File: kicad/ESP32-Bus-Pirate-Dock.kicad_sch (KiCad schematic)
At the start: 11 parts, among them J1 Conn_01x10, J4 Conn_01x22_MountingPin, J5 Conn_01x22_MountingPin, SW1 SW_BOOT, SW2 SW_RST, U1 ESP32-S3-DEVKITC-1-N8R2, U2 AMS1117-1.8

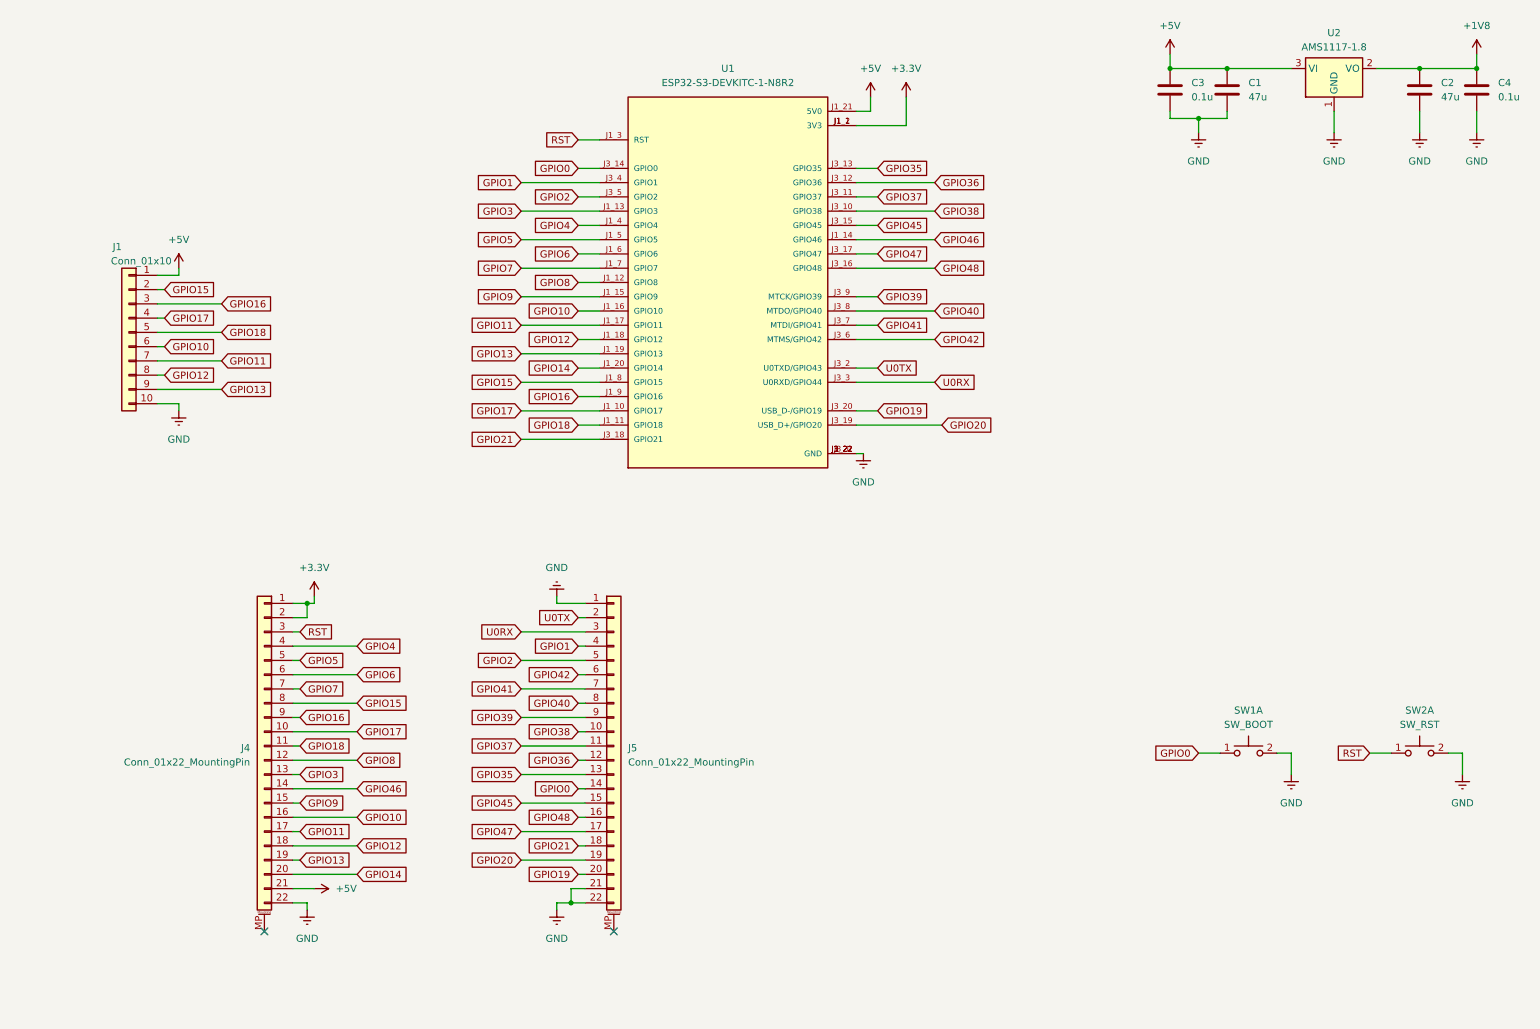
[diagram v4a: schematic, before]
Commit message: Added logic level shifting
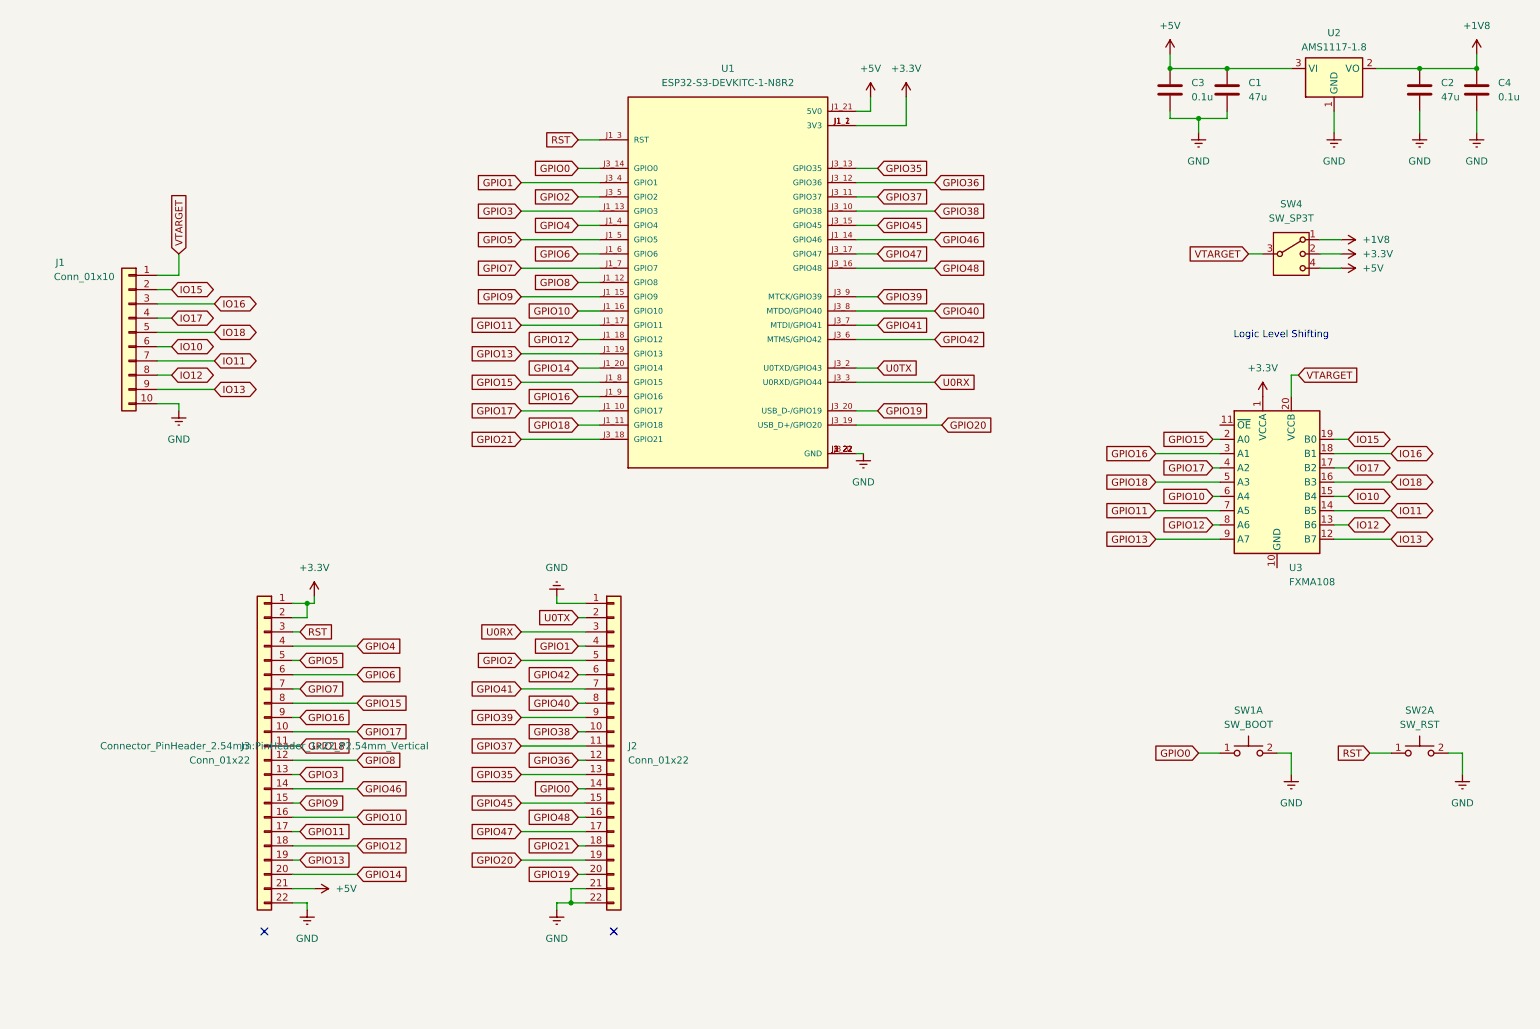
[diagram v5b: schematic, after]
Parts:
- removed J4, J5: Conn_01x22_MountingPin, Connector_PinHeader_2.54mm:PinHeader_1x22_P2.54mm_Vertical, symbol Connector_Generic_MountingPin:Conn_01x22_MountingPin
- added J2, J3: Conn_01x22, Connector_PinHeader_2.54mm:PinHeader_1x22_P2.54mm_Vertical, symbol Connector_Generic:Conn_01x22
- added SW4: SW_SP3T, Button_Switch_SMD:SW_SP3T_PCM13, symbol Switch:SW_SP3T
- added U3: FXMA108, Package_DFN_QFN:WQFN-20-1EP_2.5x4.5mm_P0.5mm_EP1x2.9mm, symbol Logic_LevelTranslator:FXMA108
- J1: footprint Connector_PinSocket_2.54mm:PinSocket_1x10_P2.54mm_Horizontal -> Connector_PinSocket_2.54mm:PinSocket_1x10_P2.54mm_Vertical
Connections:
- net +1V8: now also SW4.1
- net +3.3V: now also J3.1 (Pin_1), J3.2 (Pin_2), SW4.2, U3.1 (VCCA)
- net +5V: now also J3.21 (Pin_21), SW4.4; no longer J1.1 (Pin_1)
- net GND: now also J2.1 (Pin_1), J2.21 (Pin_21), J2.22 (Pin_22), J3.22 (Pin_22)
- net GPIO0: now also J2.14 (Pin_14)
- net GPIO1: now also J2.4 (Pin_4)
- net GPIO10: now also J3.16 (Pin_16), U3.6 (A4); no longer J1.6 (Pin_6)
- net GPIO11: now also J3.17 (Pin_17), U3.7 (A5); no longer J1.7 (Pin_7)
- net GPIO12: now also J3.18 (Pin_18), U3.8 (A6); no longer J1.8 (Pin_8)
- net GPIO13: now also J3.19 (Pin_19), U3.9 (A7); no longer J1.9 (Pin_9)
- net GPIO14: now also J3.20 (Pin_20)
- net GPIO15: now also J3.8 (Pin_8), U3.2 (A0); no longer J1.2 (Pin_2)
- net GPIO16: now also J3.9 (Pin_9), U3.3 (A1); no longer J1.3 (Pin_3)
- net GPIO17: now also J3.10 (Pin_10), U3.4 (A2); no longer J1.4 (Pin_4)
- net GPIO18: now also J3.11 (Pin_11), U3.5 (A3); no longer J1.5 (Pin_5)
- net GPIO19: now also J2.20 (Pin_20)
- net GPIO2: now also J2.5 (Pin_5)
- net GPIO20: now also J2.19 (Pin_19)
- net GPIO21: now also J2.18 (Pin_18)
- net GPIO3: now also J3.13 (Pin_13)
- net GPIO35: now also J2.13 (Pin_13)
- net GPIO36: now also J2.12 (Pin_12)
- net GPIO37: now also J2.11 (Pin_11)
- net GPIO38: now also J2.10 (Pin_10)
- net GPIO39: now also J2.9 (Pin_9)
- net GPIO4: now also J3.4 (Pin_4)
- net GPIO40: now also J2.8 (Pin_8)
- net GPIO41: now also J2.7 (Pin_7)
- net GPIO42: now also J2.6 (Pin_6)
- net GPIO45: now also J2.15 (Pin_15)
- net GPIO46: now also J3.14 (Pin_14)
- net GPIO47: now also J2.17 (Pin_17)
- net GPIO48: now also J2.16 (Pin_16)
- net GPIO5: now also J3.5 (Pin_5)
- net GPIO6: now also J3.6 (Pin_6)
- net GPIO7: now also J3.7 (Pin_7)
- net GPIO8: now also J3.12 (Pin_12)
- net GPIO9: now also J3.15 (Pin_15)
- net RST: now also J3.3 (Pin_3)
- net U0RX: now also J2.3 (Pin_3)
- net U0TX: now also J2.2 (Pin_2)
- new net IO10: J1.6 (Pin_6), U3.15 (B4)
- new net IO11: J1.7 (Pin_7), U3.14 (B5)
- new net IO12: J1.8 (Pin_8), U3.13 (B6)
- new net IO13: J1.9 (Pin_9), U3.12 (B7)
- new net IO15: J1.2 (Pin_2), U3.19 (B0)
- new net IO16: J1.3 (Pin_3), U3.18 (B1)
- new net IO17: J1.4 (Pin_4), U3.17 (B2)
- new net IO18: J1.5 (Pin_5), U3.16 (B3)
- new net VTARGET: J1.1 (Pin_1), SW4.3, U3.20 (VCCB)
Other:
- note added: "Logic Level Shifting"

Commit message: PCB modifications
- removed RESET switch
- re-arranged FXMA108 pins
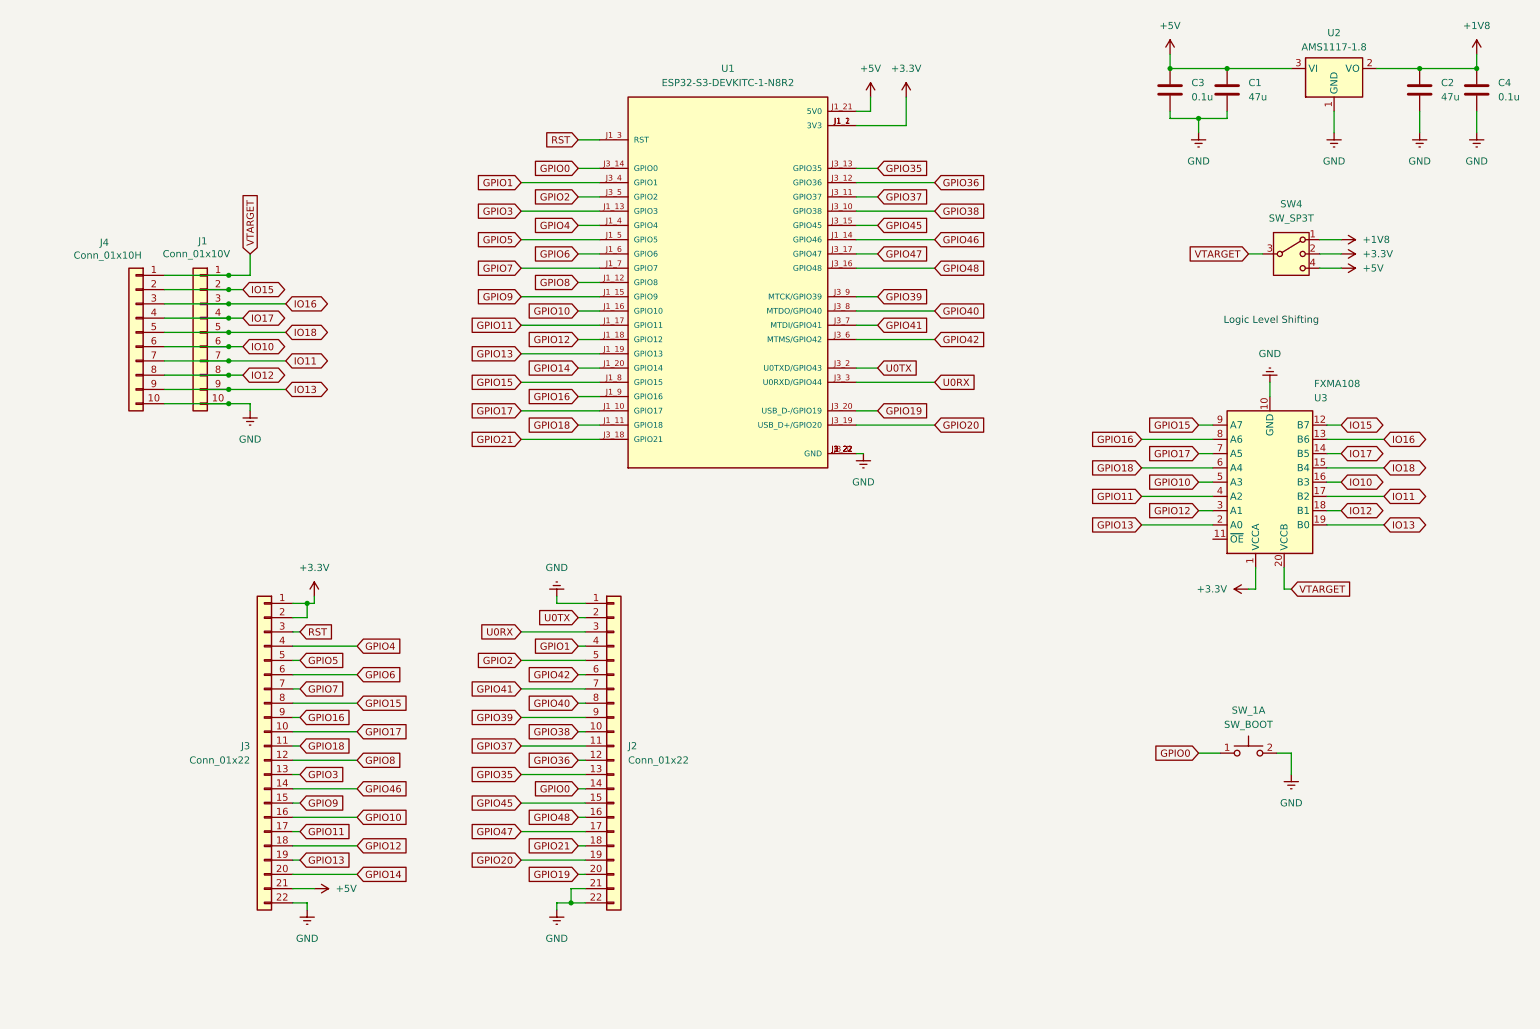
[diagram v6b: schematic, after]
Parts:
- removed SW2: SW_RST, symbol Switch:SW_Push_Dual_x2
- added J4: Conn_01x10H, Connector_PinSocket_2.54mm:PinSocket_1x10_P2.54mm_Horizontal, symbol Connector_Generic:Conn_01x10
- J1: value Conn_01x10 -> Conn_01x10V
- SW_1: renamed from SW1; footprint (none) -> Button_Switch_SMD:SW_SPST_PTS647_Sx50
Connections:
- net GND: now also U3.10 (GND), J4.10 (Pin_10)
- net GPIO10: now also U3.5 (A3); no longer U3.6 (A4)
- net GPIO11: now also U3.4 (A2); no longer U3.7 (A5)
- net GPIO12: now also U3.3 (A1); no longer U3.8 (A6)
- net GPIO13: now also U3.2 (A0); no longer U3.9 (A7)
- net GPIO15: now also U3.9 (A7); no longer U3.2 (A0)
- net GPIO16: now also U3.8 (A6); no longer U3.3 (A1)
- net GPIO17: now also U3.7 (A5); no longer U3.4 (A2)
- net GPIO18: now also U3.6 (A4); no longer U3.5 (A3)
- net IO10: now also U3.16 (B3), J4.6 (Pin_6); no longer U3.15 (B4)
- net IO11: now also U3.17 (B2), J4.7 (Pin_7); no longer U3.14 (B5)
- net IO12: now also U3.18 (B1), J4.8 (Pin_8); no longer U3.13 (B6)
- net IO13: now also U3.19 (B0), J4.9 (Pin_9); no longer U3.12 (B7)
- net IO15: now also U3.12 (B7), J4.2 (Pin_2); no longer U3.19 (B0)
- net IO16: now also U3.13 (B6), J4.3 (Pin_3); no longer U3.18 (B1)
- net IO17: now also U3.14 (B5), J4.4 (Pin_4); no longer U3.17 (B2)
- net IO18: now also U3.15 (B4), J4.5 (Pin_5); no longer U3.16 (B3)
- net VTARGET: now also J4.1 (Pin_1)
- no-connect marks 2 -> 0
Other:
- moved on the sheet: J1, U3

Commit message: PCB arrangement
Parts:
- added H1, H2, H3, H4: MountingHole, MountingHole:MountingHole_3.2mm_M3, symbol Mechanical:MountingHole
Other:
- moved on the sheet: C1, C2, C3, C4, J1, J2, J3, J4, SW4, U1, U2, U3

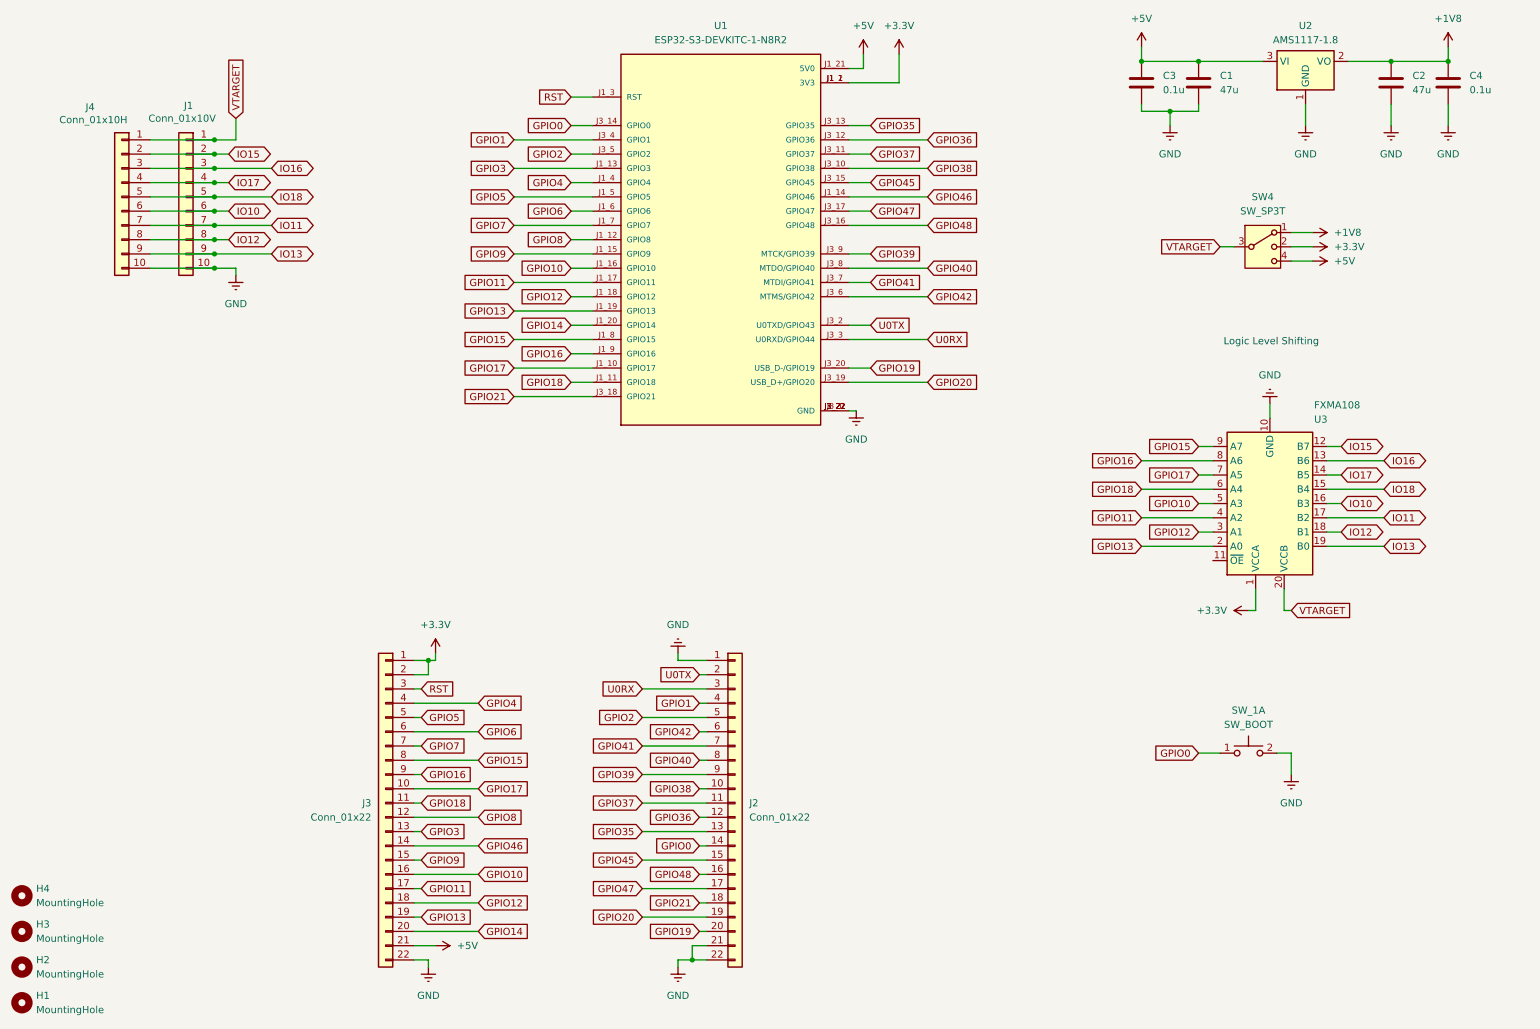
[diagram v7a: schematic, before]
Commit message: Added DP3T switch in schematic
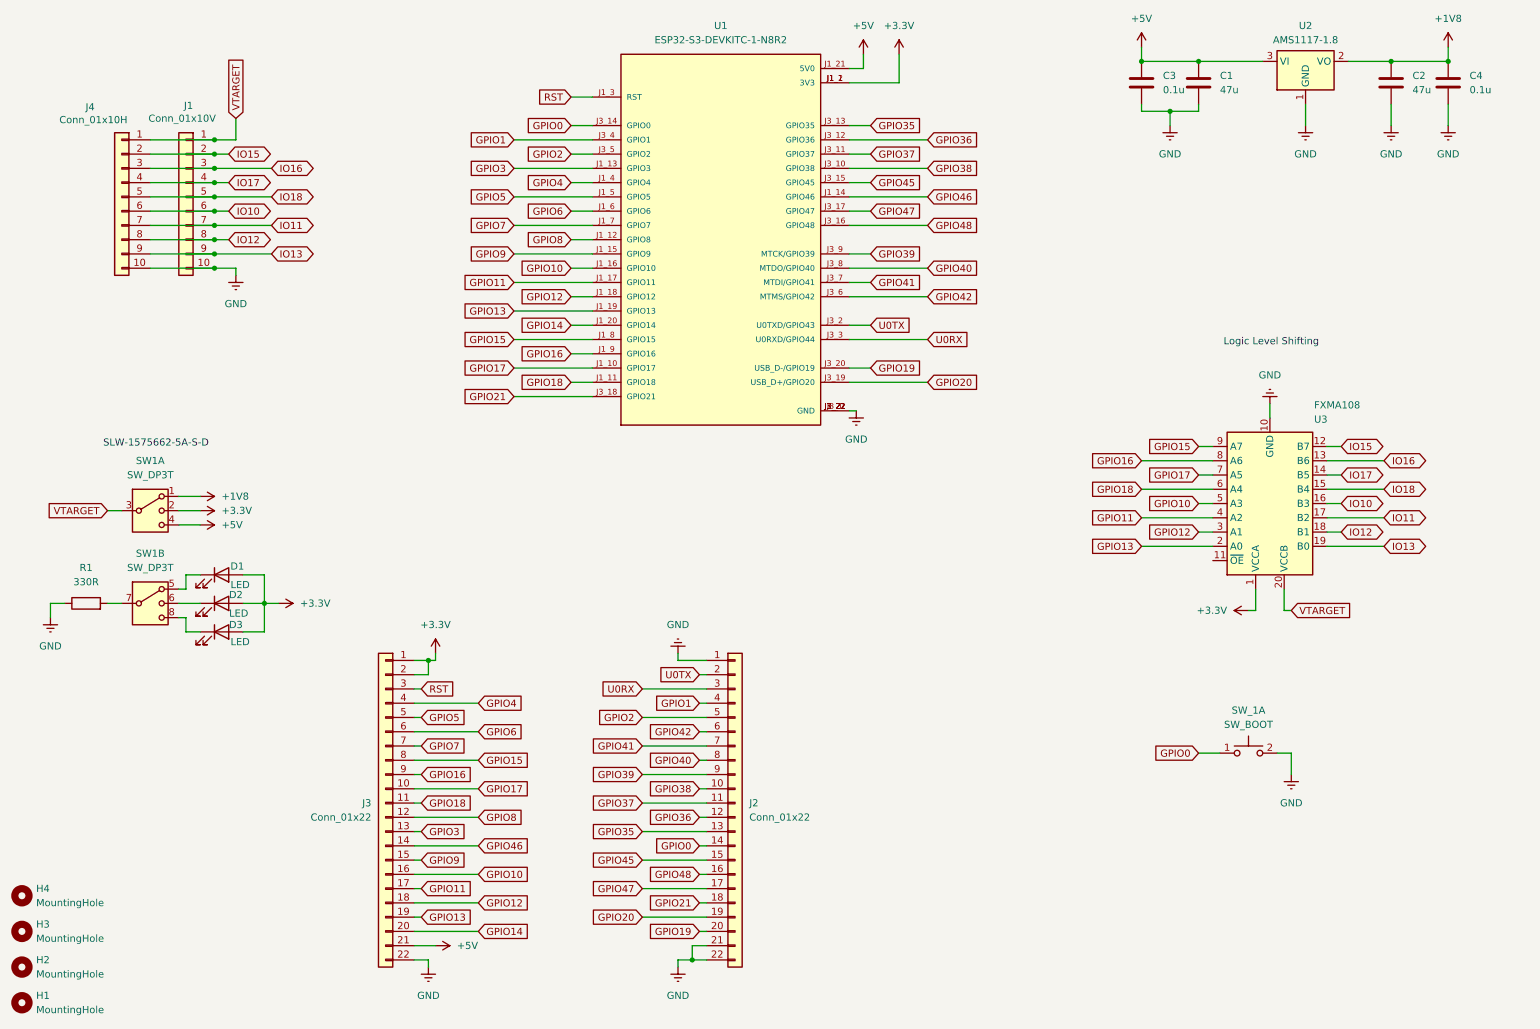
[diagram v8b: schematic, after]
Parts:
- removed SW4: SW_SP3T, Button_Switch_SMD:SW_SP3T_PCM13, symbol Switch:SW_SP3T
- added D1, D2, D3: LED, LED_SMD:LED_0805_2012Metric, symbol Device:LED
- added R1: 330R, Resistor_SMD:R_0805_2012Metric, symbol Device:R
- added SW1: SW_DP3T, symbol Switch:SW_DP3T
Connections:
- net +1V8: now also SW1.1
- net +3.3V: now also D1.2 (A), D2.2 (A), D3.2 (A), SW1.2
- net +5V: now also SW1.4
- net GND: now also R1.1
- net VTARGET: now also SW1.3
- new net: R1.2, SW1.7
- new net: D3.1 (K), SW1.8
- new net: D1.1 (K), SW1.5
- new net: D2.1 (K), SW1.6
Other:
- note added: "SLW-1575662-5A-S-D"
